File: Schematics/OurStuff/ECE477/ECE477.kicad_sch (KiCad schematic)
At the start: 6 parts, among them J1 USB_B_Micro, U1 ESP32-WROOM-32E, U2 CP2102N-Axx-xQFN28

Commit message: fixed power
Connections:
- net VBUS renamed V_BUS
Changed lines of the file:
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@@
-		)
-	)
-	(label "VBUS"
-		(at 60.96 152.4 0)
-		(fields_autoplaced yes)
-		(effects
-			(font
-				(size 1.27 1.27)
-			)
-			(justify left bottom)
 		)
 	)
 	(label "USB_DN"
 		(at 66.04 140.97 0)
-		(fields_autoplaced yes)
-		(effects
-			(font
-				(size 1.27 1.27)
-			)
-			(justify left bottom)
-		)
-	)
-	(label "VBUS"
-		(at 66.04 138.43 0)
 		(fields_autoplaced yes)
 		(effects
@@
 		)
 	)
+	(global_label "V_BUS"
+		(shape input)
+		(at 66.04 138.43 180)
+		(fields_autoplaced yes)
+		(effects
+			(font
+				(size 1.27 1.27)
+			)
+			(justify right)
+		)
+		(property "Intersheetrefs" "${INTERSHEET_REFS}"
+			(at 57.1886 138.43 0)
+			(effects
+				(font
+					(size 1.27 1.27)
+				)
+				(justify right)
+				(hide yes)
+			)
+		)
+	)
+	(global_label "V_BUS"
+		(shape input)
+		(at 60.96 152.4 0)
+		(fields_autoplaced yes)
+		(effects
+			(font
+				(size 1.27 1.27)
+			)
+			(justify left)
+		)
+		(property "Intersheetrefs" "${INTERSHEET_REFS}"
+			(at 69.8114 152.4 0)
+			(effects
+				(font
+					(size 1.27 1.27)
+				)
+				(justify left)
+				(hide yes)
+			)
+		)
+	)

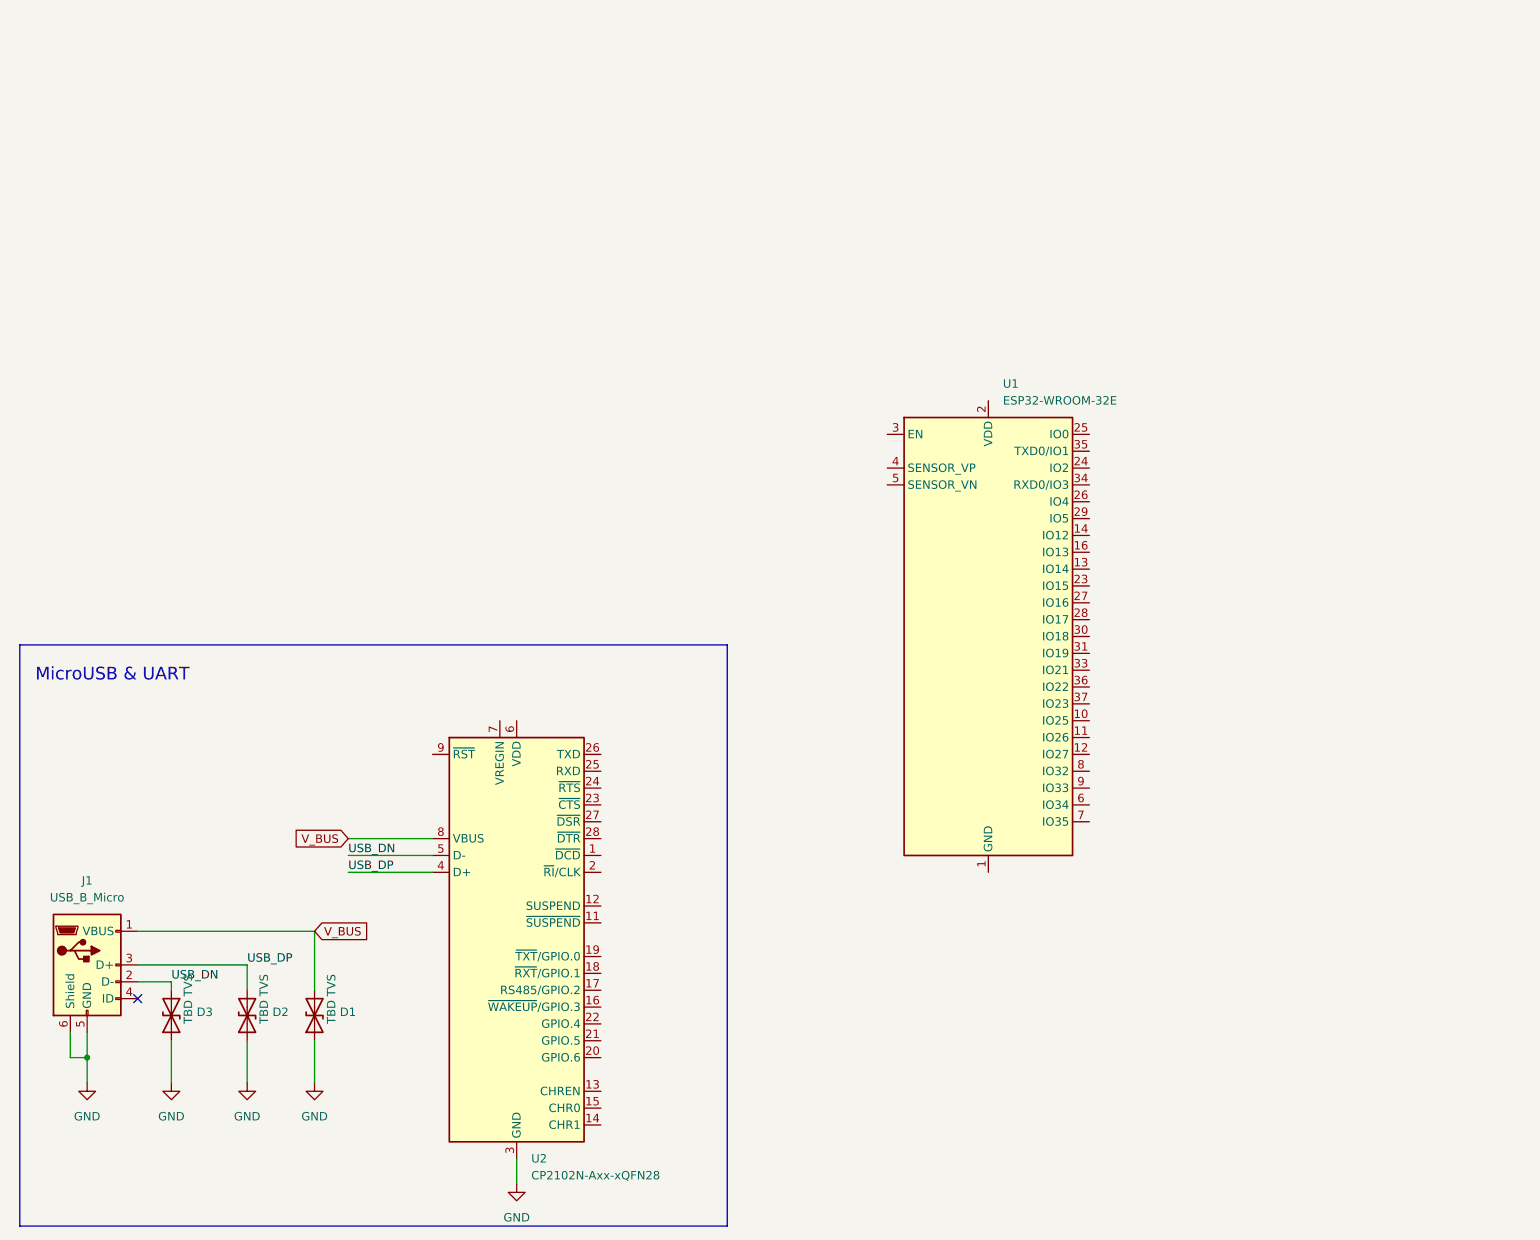
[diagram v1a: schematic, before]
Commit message: Finished UART
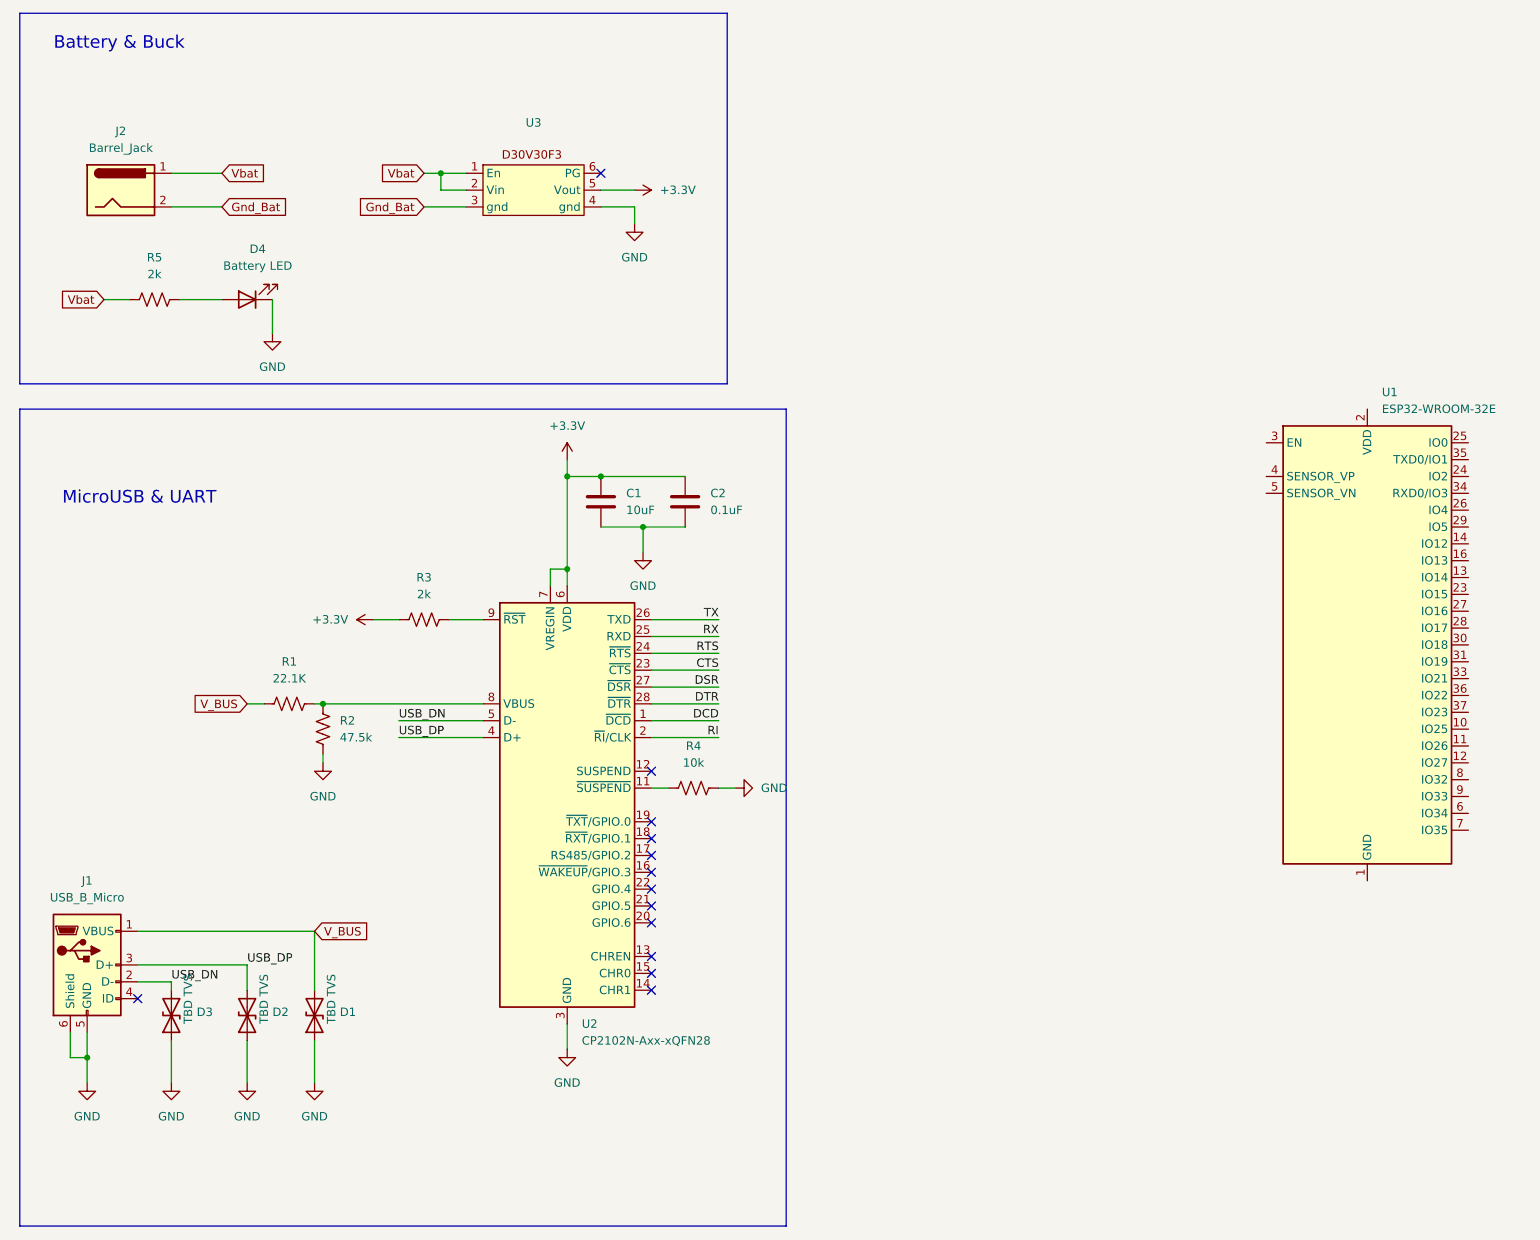
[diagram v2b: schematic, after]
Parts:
- added C1: 10uF, symbol Device:C
- added C2: 0.1uF, symbol Device:C
- added D4: Battery LED, symbol Device:LED
- added J2: Barrel_Jack, symbol Connector:Barrel_Jack
- added R1: 22.1K, symbol Device:R_US
- added R2: 47.5k, symbol Device:R_US
- added R3, R5: 2k, symbol Device:R_US
- added R4: 10k, symbol Device:R_US
- added U3: ~, symbol D30V30F3:D30V30F3
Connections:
- net GND: now also C1.2, C2.2, D4.1 (K), R2.2, R4.1, U3.4 (gnd)
- net V_BUS: now also R1.2; no longer U2.8 (VBUS)
- net DCD: now reaches U2.1 (~{DCD})
- net at U2.11 (~{SUSPEND}): now also R4.2
- net RI: now reaches U2.2 (~{RI}/CLK)
- net CTS: now reaches U2.23 (~{CTS})
- net RTS: now reaches U2.24 (~{RTS})
- net RX: now reaches U2.25 (RXD)
- net TX: now reaches U2.26 (TXD)
- net DSR: now reaches U2.27 (~{DSR})
- net DTR: now reaches U2.28 (~{DTR})
- net +3.3V: now reaches U2.6 (VDD)
- net +3.3V: now also U2.7 (VREGIN), C1.1, C2.1, R3.2, U3.5 (Vout)
- net at U2.9 (~{RST}): now also R3.1
- new net: R1.1, R2.1, U2.8 (VBUS)
- new net: D4.2 (A), R5.2
- new net Gnd_Bat: J2.2, U3.3 (gnd)
- new net Vbat: J2.1, R5.1, U3.1 (En), U3.2 (Vin)
- no-connect marks 1 -> 13
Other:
- note added: "Battery & Buck"
- moved on the sheet: U1, U2

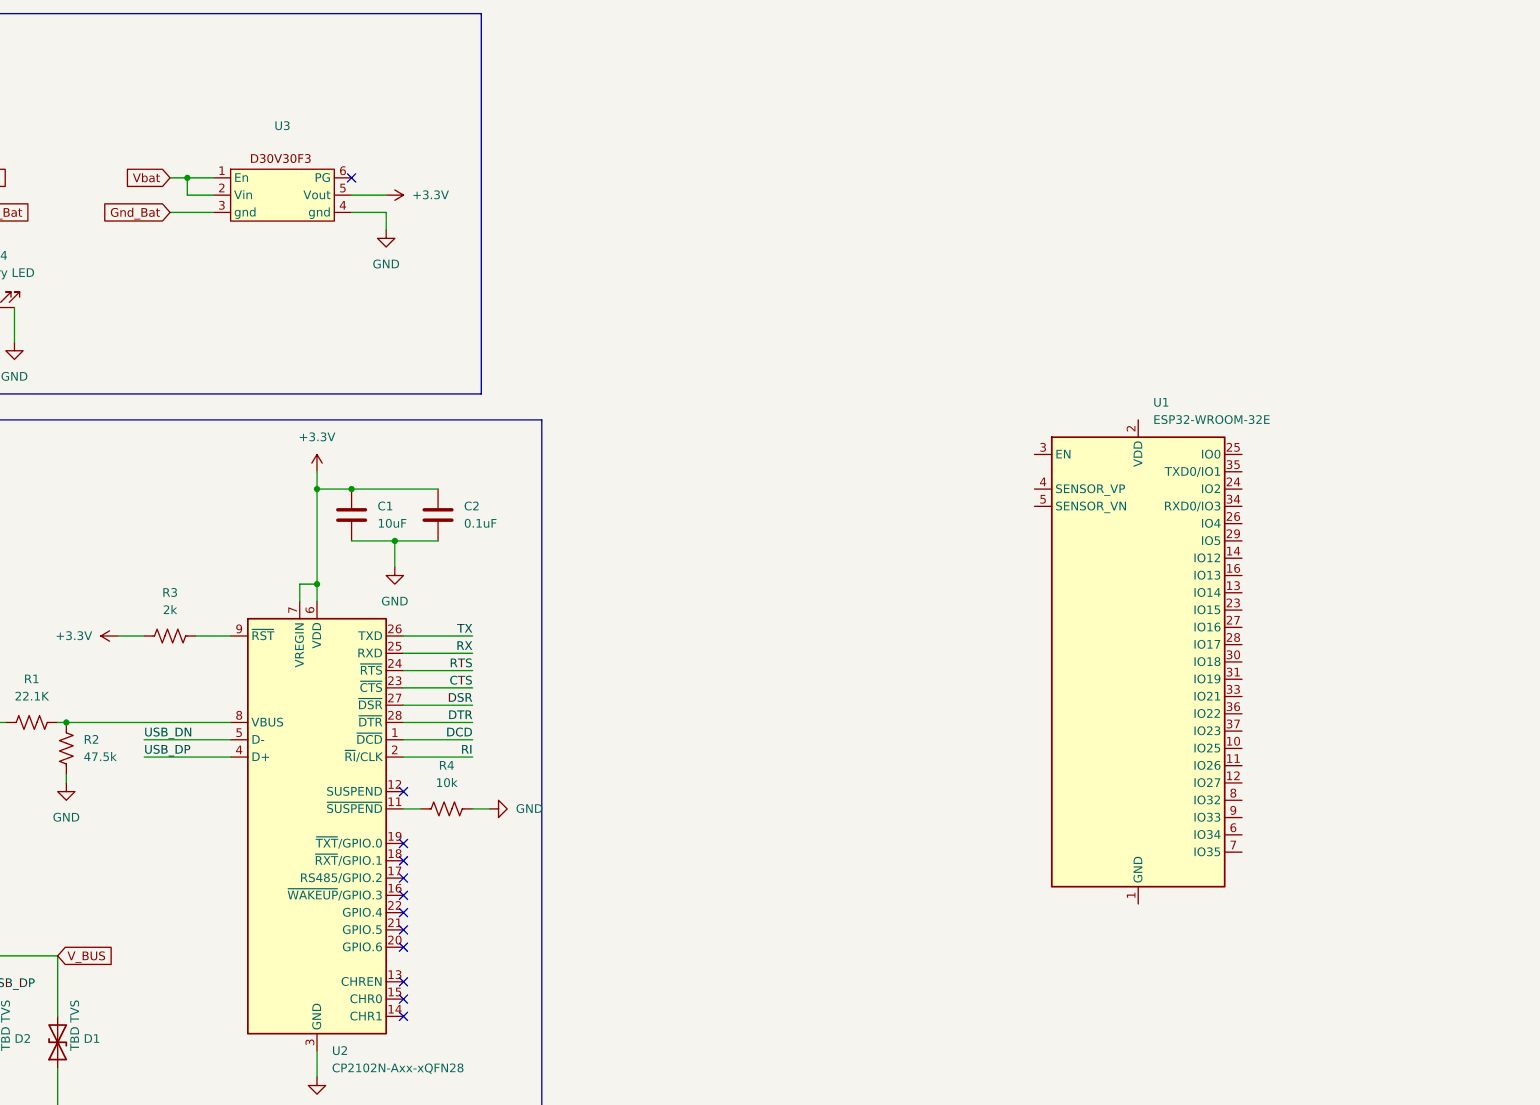
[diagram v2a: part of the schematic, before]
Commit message: added auto flash circuitry
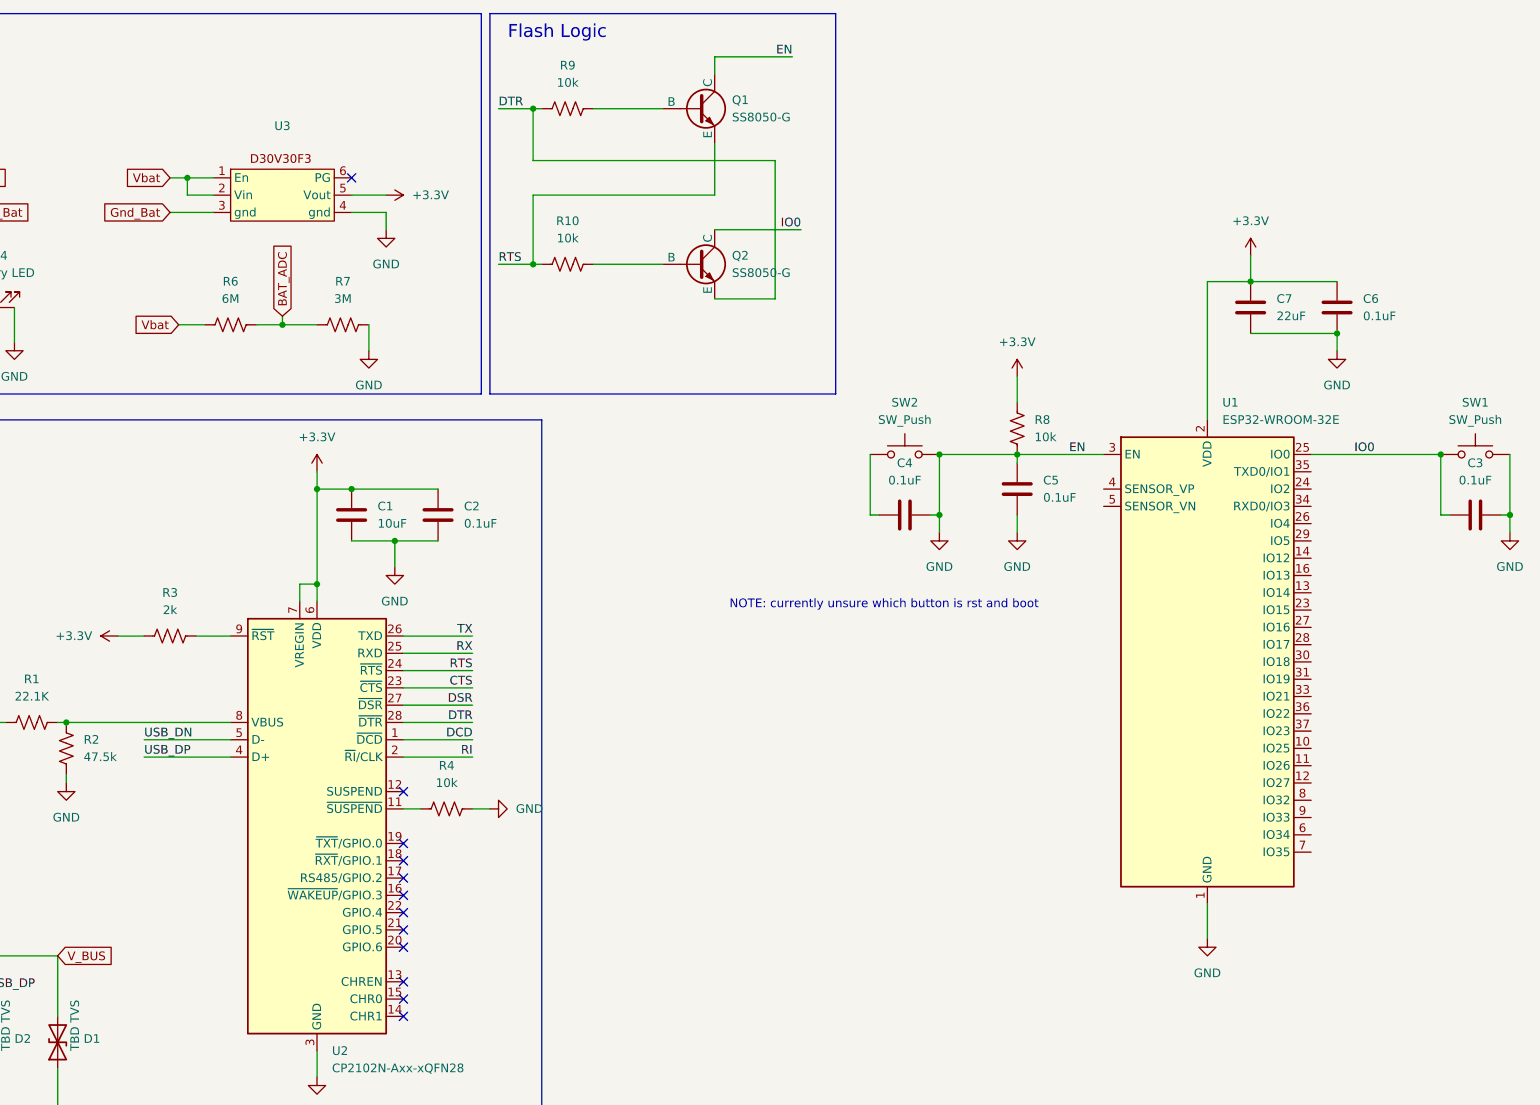
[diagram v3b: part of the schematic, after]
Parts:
- added C3, C4, C5, C6: 0.1uF, symbol Device:C
- added C7: 22uF, symbol Device:C
- added Q1, Q2: SS8050-G, symbol Simulation_SPICE:NPN
- added R10, R8, R9: 10k, symbol Device:R_US
- added R6: 6M, symbol Device:R_US
- added R7: 3M, symbol Device:R_US
- added SW1, SW2: SW_Push, symbol Switch:SW_Push
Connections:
- net +3.3V: now also U1.2 (VDD), C6.1, C7.1, R8.2
- net DTR: now also Q2.3 (E), R9.2
- net GND: now also U1.1 (GND), U1.15 (GND), U1.3 (EN), U1.38 (GND), U1.39 (GND), C3.1, C4.1, C5.1, C5.2, C6.2, C7.2, Q1.1 (C), R7.2, R8.1, SW1.2, SW2.2
- net RTS: now also Q1.3 (E), R10.2
- net Vbat: now also R6.1
- net IO0: now reaches U1.25 (IO0)
- net IO0: now also C3.2, Q2.1 (C), SW1.1
- new net: Q2.2 (B), R10.1
- new net: C4.2, SW2.1
- new net: Q1.2 (B), R9.1
- new net BAT_ADC: R6.2, R7.1
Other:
- note added: "Flash Logic"
- note added: "NOTE: currently unsure which button is rst and boot"
- moved on the sheet: U1

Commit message: Added Peripherals
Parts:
- added C8, C9: 0.1uF, symbol Device:C
- added J3: OLED JST PH 7pin, symbol Connector:Conn_01x07_Socket
- added J4: Microphone Connector, symbol Connector:Conn_01x03_Socket
- added SW3: Button 1, symbol Switch:SW_Push_Dual
- added SW4: Button 2, symbol Switch:SW_Push_Dual
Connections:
- net +3.3V: now also J3.1 (Pin_1)
- net GND: now also C8.2, C9.2, J3.2 (Pin_2), SW3.2, SW3.4, SW4.2, SW4.4
- new net Button1: C8.1, SW3.1, SW3.3
- new net Button2: C9.1, SW4.1, SW4.3
- new net O_CLK: J3.4 (Pin_4)
- new net O_CS: J3.5 (Pin_5)
- new net O_DC: J3.6 (Pin_6)
- new net O_DIN: J3.3 (Pin_3)
- new net O_RST: J3.7 (Pin_7)
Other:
- note added: "ESP32 + Support Circuitry"
- note added: "Note: buttons assumed to be using internal pullup"
- note added: "OLED 7PIN Connector (CHECK POLARITY)"
- note added: "Peripherals"
- note added: "TBD on MIC Connector"
- moved on the sheet: C3, C4, C5, C6, C7, R8, SW1, SW2, U1

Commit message: added debug
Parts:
- removed C5: 0.1uF, symbol Device:C
- added D5: Power LED, symbol Device:LED
- added D6: TX_LED, symbol Device:LED
- added D7, D8, D9: RX_LED, symbol Device:LED
- added J5, J6: Conn_01x02_Pin, symbol Connector:Conn_01x02_Pin
- added R11, R12: 10k, symbol Device:R_US
- added R13, R15, R16, R17, R18: 220, symbol Device:R_US
- D1, D2, D3: value TBD TVS -> ESD9B5.0ST5G
- SW1: value SW_Push -> Boot Button
- SW2: value SW_Push -> RST Button
- U3: value ~ -> D30V30F3
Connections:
- net +3.3V: now also J4.3 (Pin_3), R11.1, R12.1, R13.1
- net Button1: now also R11.2
- net Button2: now also R12.2
- net GND: now also C4.2, J4.2 (Pin_2), SW2.1, D5.1 (K), D6.1 (K), D7.1 (K), D8.1 (K), D9.1 (K); no longer C4.1, J1.6 (Shield), Q1.1 (C), R8.1, SW2.2, U1.3 (EN)
- net O_CLK: now also U1.30 (IO18)
- net O_CS: now also U1.33 (IO21)
- net O_DC: now also U1.31 (IO19)
- net O_DIN: now also U1.37 (IO23)
- net O_RST: now also U1.36 (IO22)
- net RX: now also U1.34 (RXD0/IO3), J5.2 (Pin_2), R16.1
- net TX: now also U1.35 (TXD0/IO1), J5.1 (Pin_1), R15.1
- net Vbat: now also U1.4 (SENSOR_VP)
- net Mic_In: now reaches J4.1 (Pin_1)
- net Mic_In: now also U1.6 (IO34)
- net Debug_1: now reaches U1.10 (IO25)
- net Debug_1: now also R17.1
- net Debug_2: now reaches U1.11 (IO26)
- net Debug_2: now also R18.1
- net Debug_3: now reaches U1.12 (IO27)
- net Debug_3: now also J6.1 (Pin_1)
- net Debug_4: now reaches U1.8 (IO32)
- net Debug_4: now also J6.2 (Pin_2)
- net CTS: no longer names the net of U2.23 (~{CTS})
- net DCD: no longer names the net of U2.1 (~{DCD})
- net DSR: no longer names the net of U2.27 (~{DSR})
- net RI: no longer names the net of U2.2 (~{RI}/CLK)
- new net: D5.2 (A), R13.2
- new net: D8.2 (A), R17.2
- new net: D7.2 (A), R16.2
- new net: D6.2 (A), R15.2
- new net: D9.2 (A), R18.2
- new net EN: C4.1, Q1.1 (C), R8.1, SW2.2, U1.3 (EN)
- no-connect marks 13 -> 30
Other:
- note added: "Buttons"
- note added: "General DEBUG"
- note added: "Note: assume gpio0-gpio17 are special and should not have anything attatched to them"
- note added: "Note: assuming the debug connectors are just header pins"
- note added: "UART DEBUG"
- note removed: "NOTE: currently unsure which button is rst and boot"
- note removed: "Note: buttons assumed to be using internal pullup"
- moved on the sheet: C1, C2, C4, C6, C7, C8, C9, D1, D2, D3, D4, J1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

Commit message: fixed issues
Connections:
- net +3.3V: now also R15.1, R16.1
- net BAT_ADC: now also U1.4 (SENSOR_VP)
- net GND: no longer D6.1 (K), D7.1 (K)
- net RX: now also D7.1 (K), U2.26 (TXD); no longer R16.1, U2.25 (RXD)
- net TX: now also D6.1 (K), U2.25 (RXD); no longer R15.1, U2.26 (TXD)
- net Vbat: no longer U1.4 (SENSOR_VP)
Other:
- moved on the sheet: D6, D7, R15, R16
